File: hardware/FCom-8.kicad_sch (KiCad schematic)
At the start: 29 parts, among them J101 Conn_01x04, SW101 SW_DIP_x08, SW102 SW_DIP_x08, SW104 SW_DIP_x04, SW105 G19AP, U101 W65C02S6TPG-14, U102 AS6C1008-55PCN, U103 W65C22N6TPG-14, U104 74LS04, U105 74LS08, U106 74LS21, Y101 ECS-100AX-010

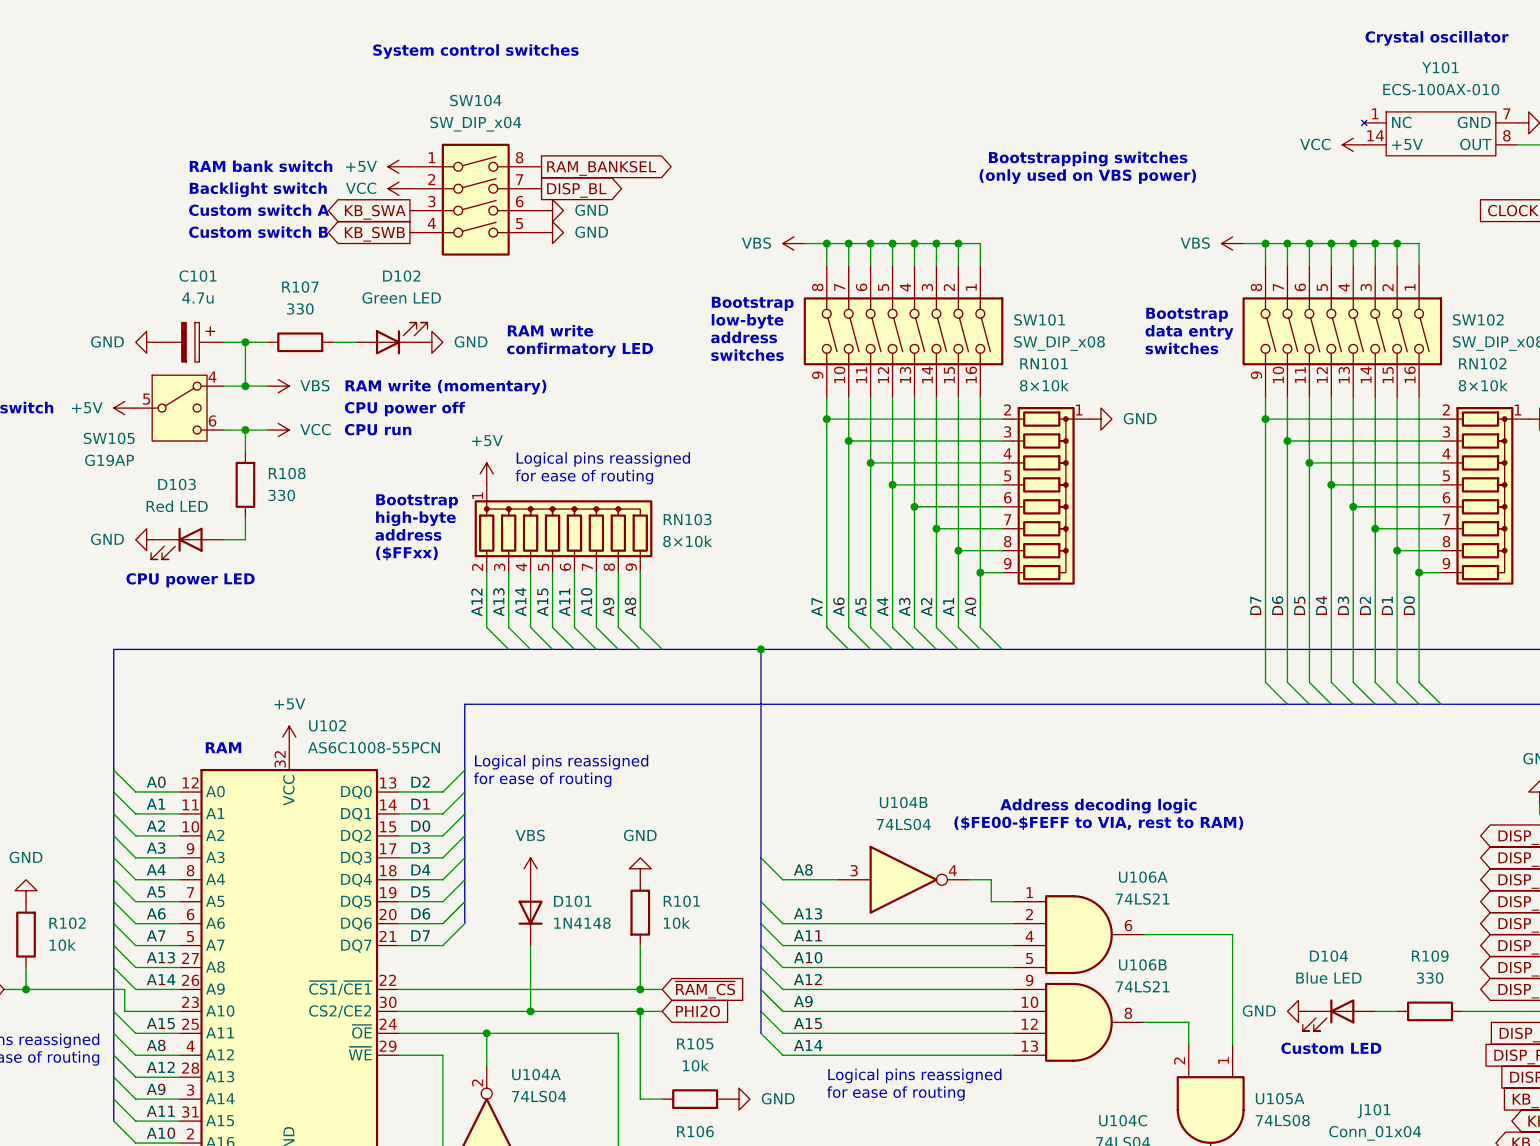
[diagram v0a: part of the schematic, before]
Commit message: Modify power circuitry to use better diode arrangement and more energy-efficient regulator
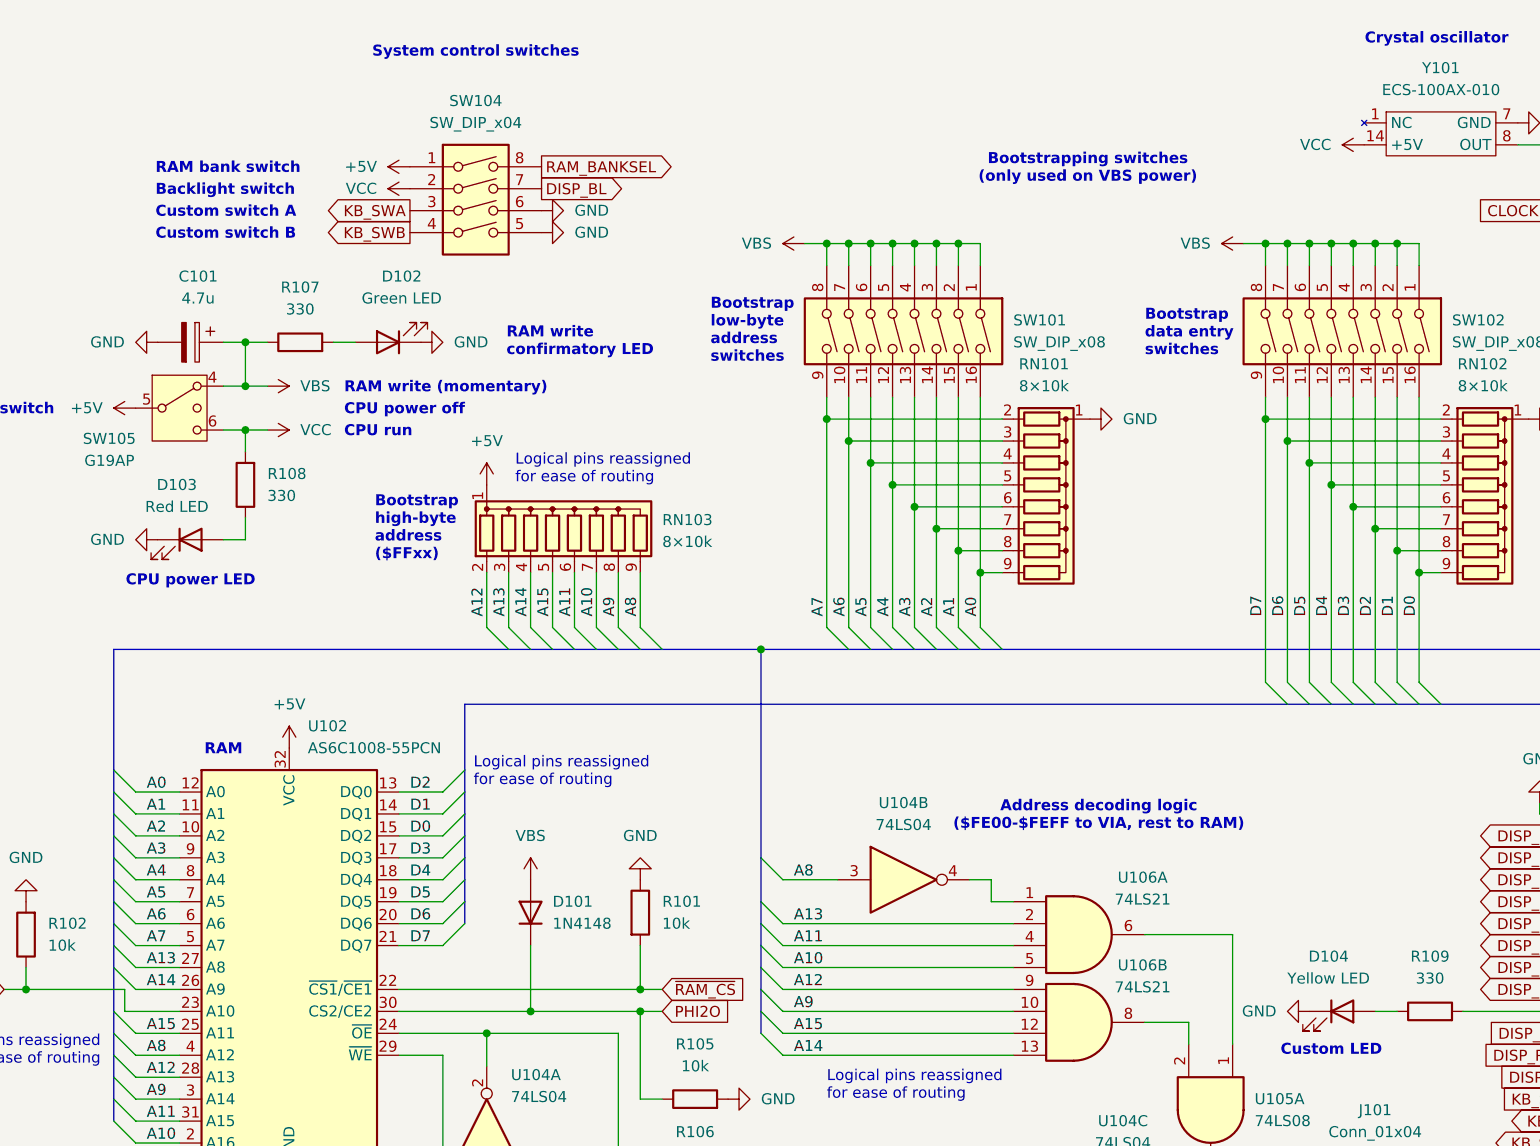
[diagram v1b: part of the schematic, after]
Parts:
- D104: value Blue LED -> Yellow LED
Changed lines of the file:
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@@
 	(text "Custom switch A"
 		(exclude_from_sim no)
-		(at 54.356 37.084 0)
+		(at 50.546 37.084 0)
 		(effects
 			(font
@@
 	(text "Backlight switch"
 		(exclude_from_sim no)
-		(at 54.356 34.544 0)
+		(at 50.546 34.544 0)
 		(effects
 			(font
@@
 	(text "RAM bank switch"
 		(exclude_from_sim no)
-		(at 54.356 32.004 0)
+		(at 50.546 32.004 0)
 		(effects
 			(font
@@
 	(text "Custom switch B"
 		(exclude_from_sim no)
-		(at 54.356 39.624 0)
+		(at 50.546 39.624 0)
 		(effects
 			(font
@@
 			)
 		)
-		(property "Value" "Blue LED"
+		(property "Value" "Yellow LED"
 			(at 186.3725 125.73 0)
 			(effects
